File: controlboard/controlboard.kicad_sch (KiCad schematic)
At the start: 9 parts, among them J1 Conn_02x08_Odd_Even, J2 Conn_02x08_Odd_Even, J3 Conn_02x05_Odd_Even, U1 74HC163, U2 74HCT245, U3 74HCT245

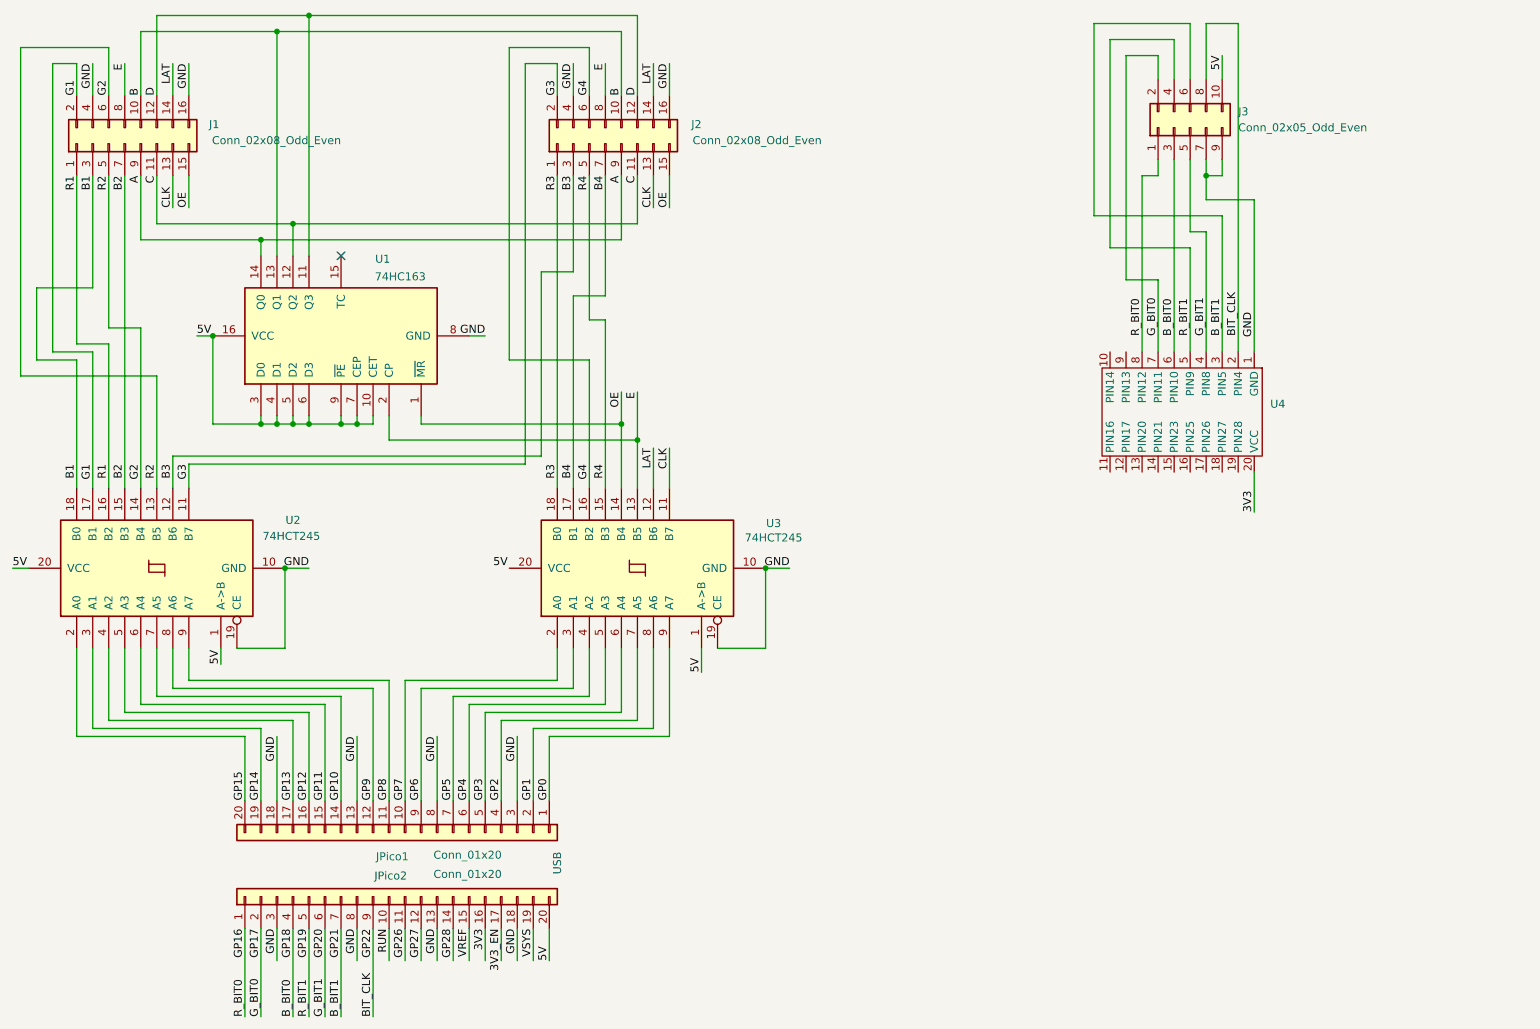
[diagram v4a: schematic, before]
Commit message: Wiring of HDMI connector
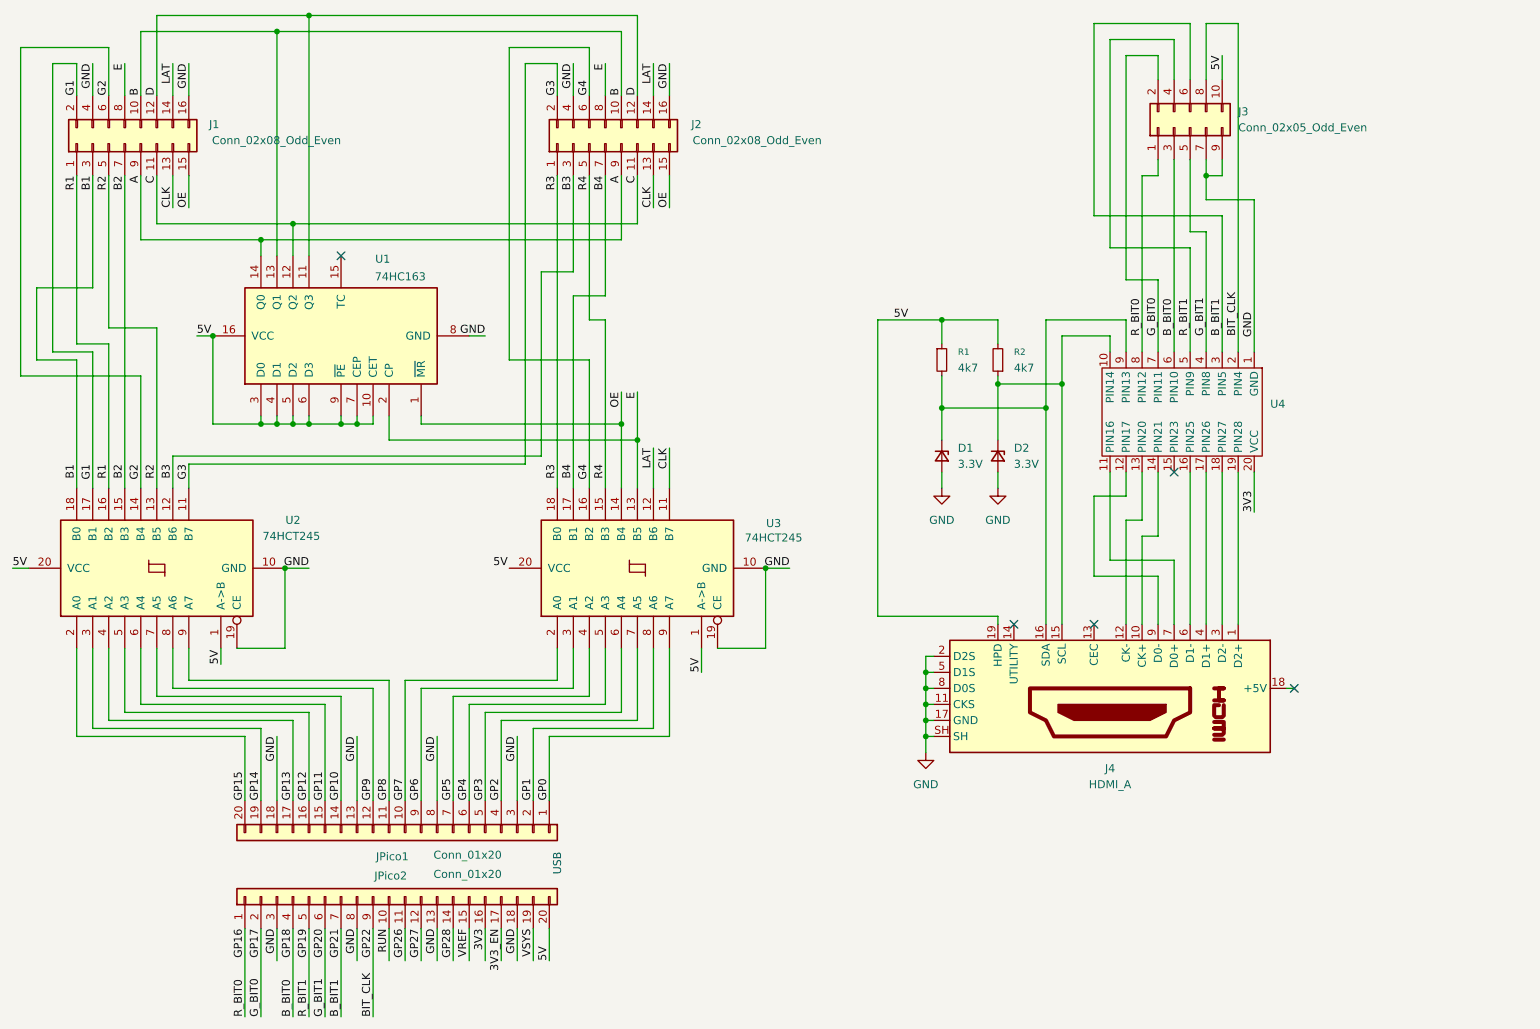
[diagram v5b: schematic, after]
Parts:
- added D1, D2: 3.3V, symbol Device:D_Zener_Small
- added J4: HDMI_A, symbol Connector:HDMI_A
- added R1, R2: 4k7, symbol Device:R_Small
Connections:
- net 5V: now also J4.19 (HPD), R1.1, R2.2
- net G2: no longer J1.5 (Pin_5), U2.13 (B5)
- net GND: now also D1.2 (A), D2.2 (A), J4.11 (CKS), J4.17 (GND), J4.2 (D2S), J4.5 (D1S), J4.8 (D0S), J4.SH
- net at U4.10 (PIN14): now also D2.1 (K), J4.15 (SCL), R2.1
- net at U4.11 (PIN16): now also J4.7 (D0+)
- net at U4.12 (PIN17): now also J4.9 (D0-)
- net at U4.13 (PIN20): now also J4.12 (CK-)
- net at U4.14 (PIN21): now also J4.10 (CK+)
- net at U4.16 (PIN25): now also J4.6 (D1-)
- net at U4.17 (PIN26): now also J4.4 (D1+)
- net at U4.18 (PIN27): now also J4.3 (D2-)
- net at U4.19 (PIN28): now also J4.1 (D2+)
- net at U4.9 (PIN13): now also D1.1 (K), J4.16 (SDA), R1.2
- new net R2: J1.5 (Pin_5), U2.13 (B5)
- no-connect marks 1 -> 5
